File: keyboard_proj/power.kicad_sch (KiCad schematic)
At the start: 18 parts, among them IC4 USBLC6-4SC6, U1 STM32WB55CGU6, U5 918-418K2023S40026

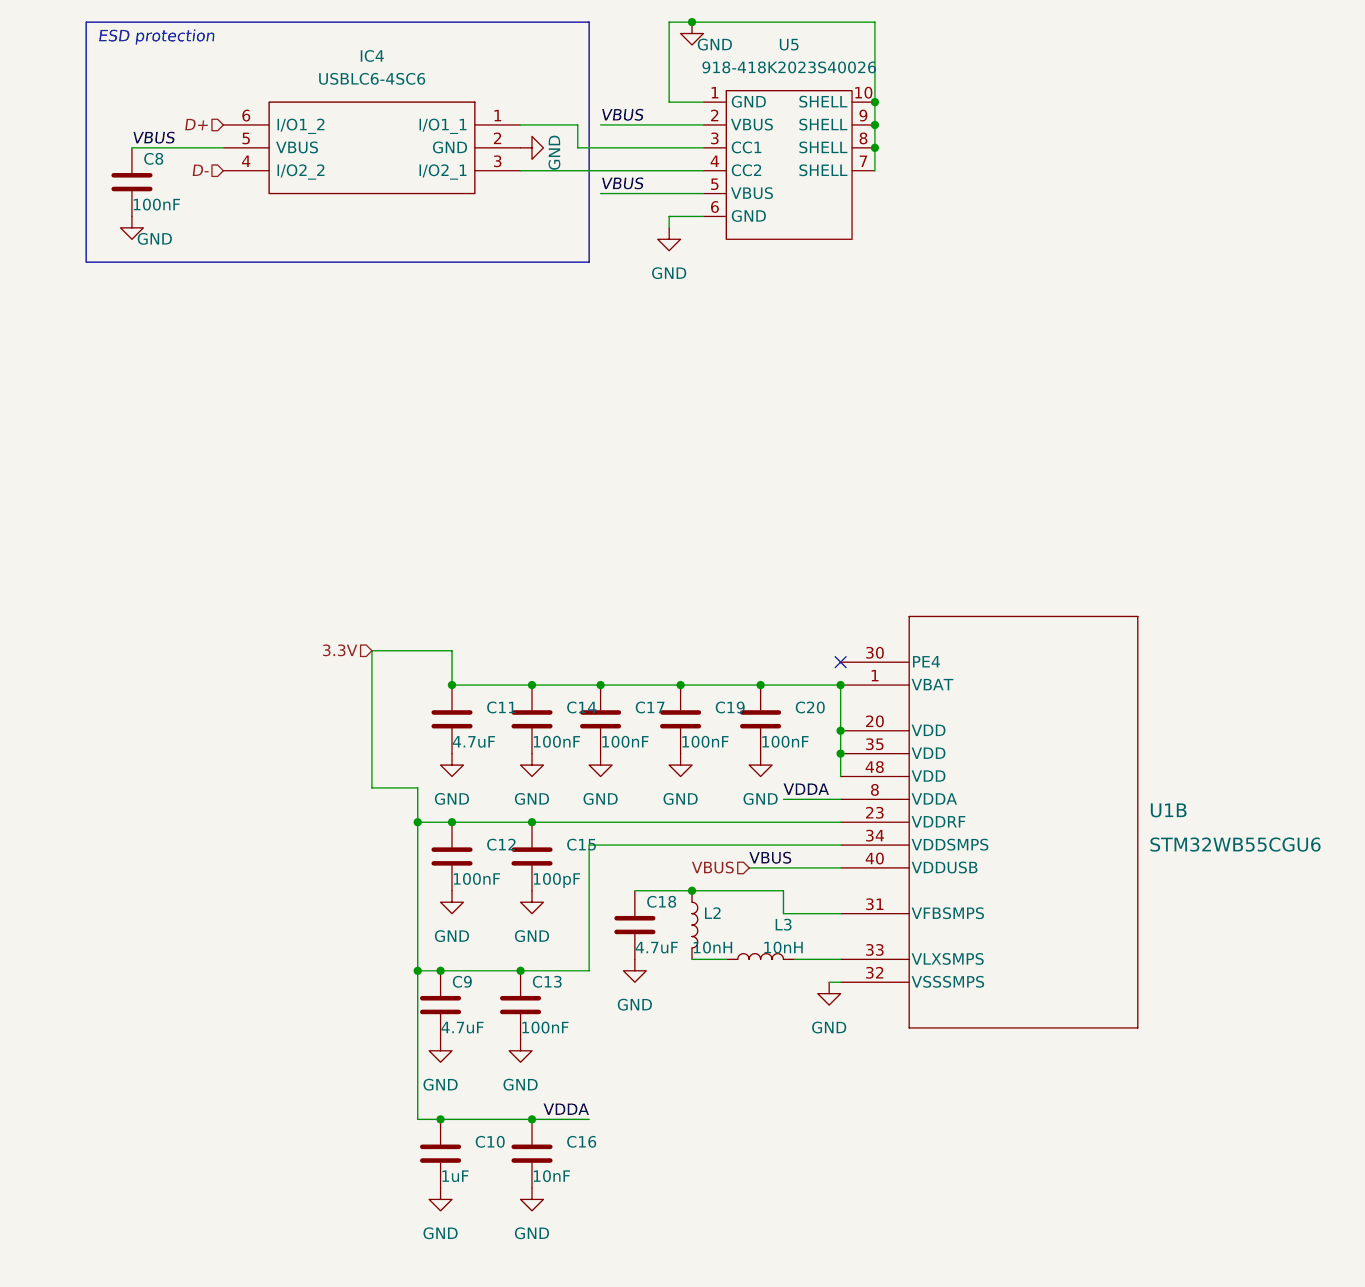
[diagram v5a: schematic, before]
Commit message: passage kicad 7, routing bien avancé
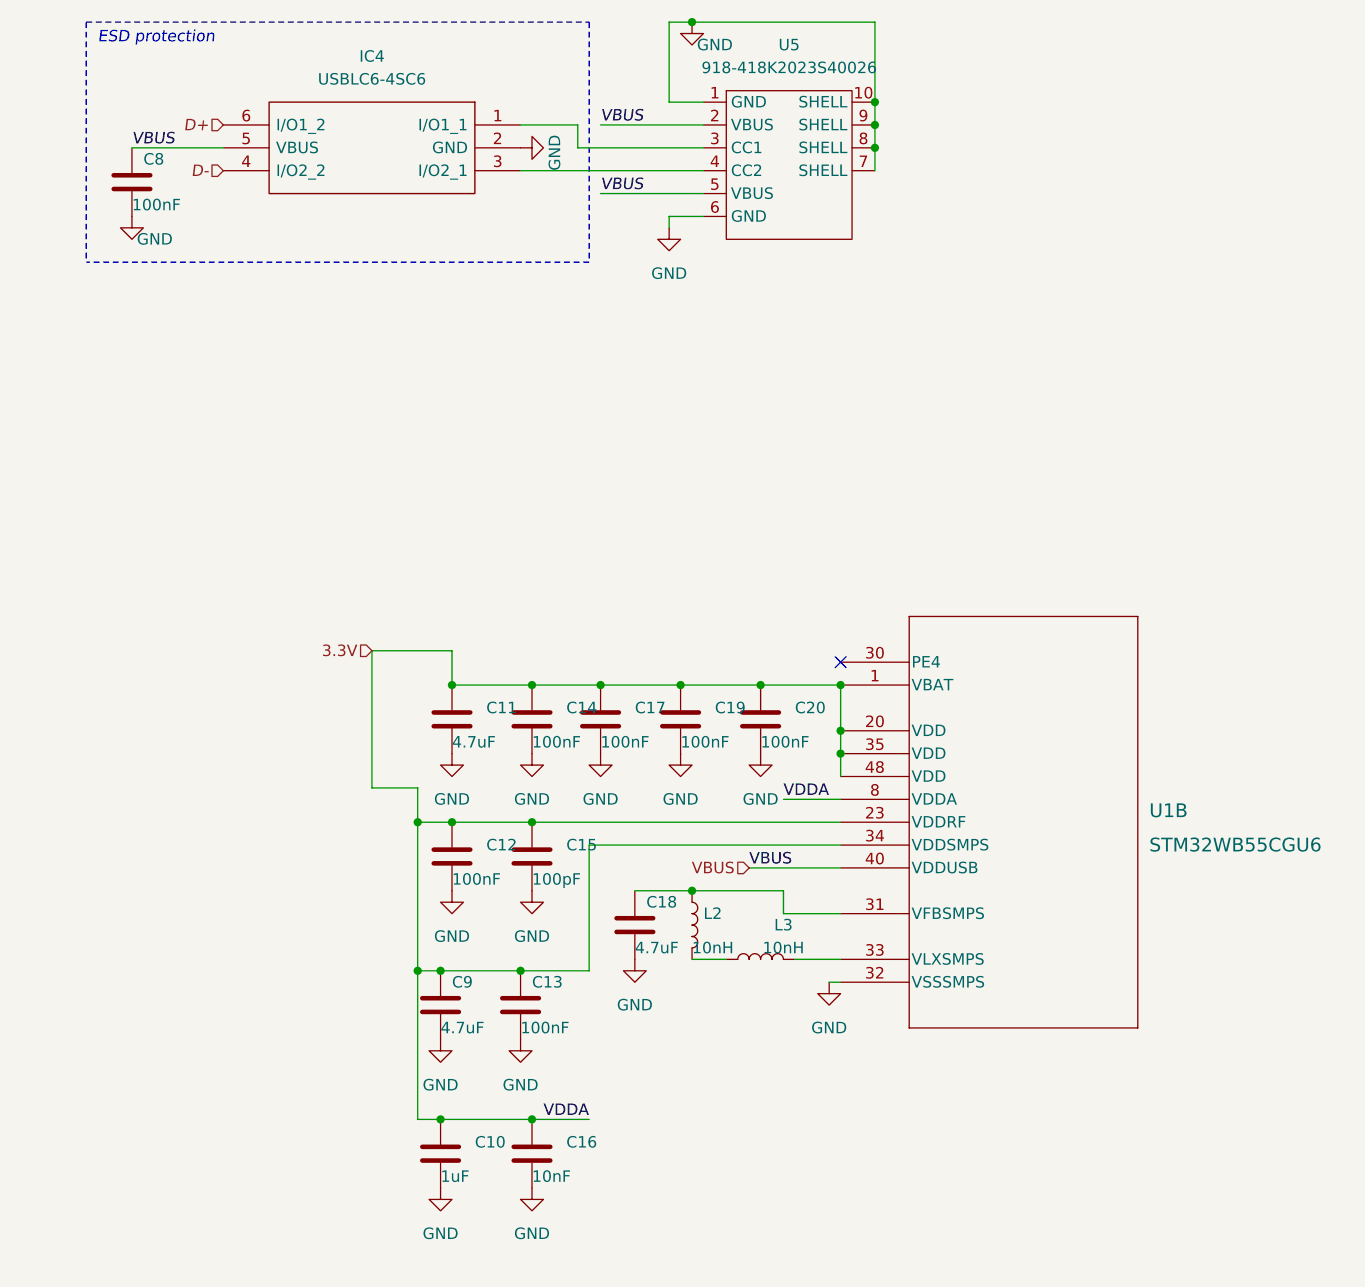
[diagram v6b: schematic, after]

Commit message: Power dlvry changée, ok mtn, routing updated
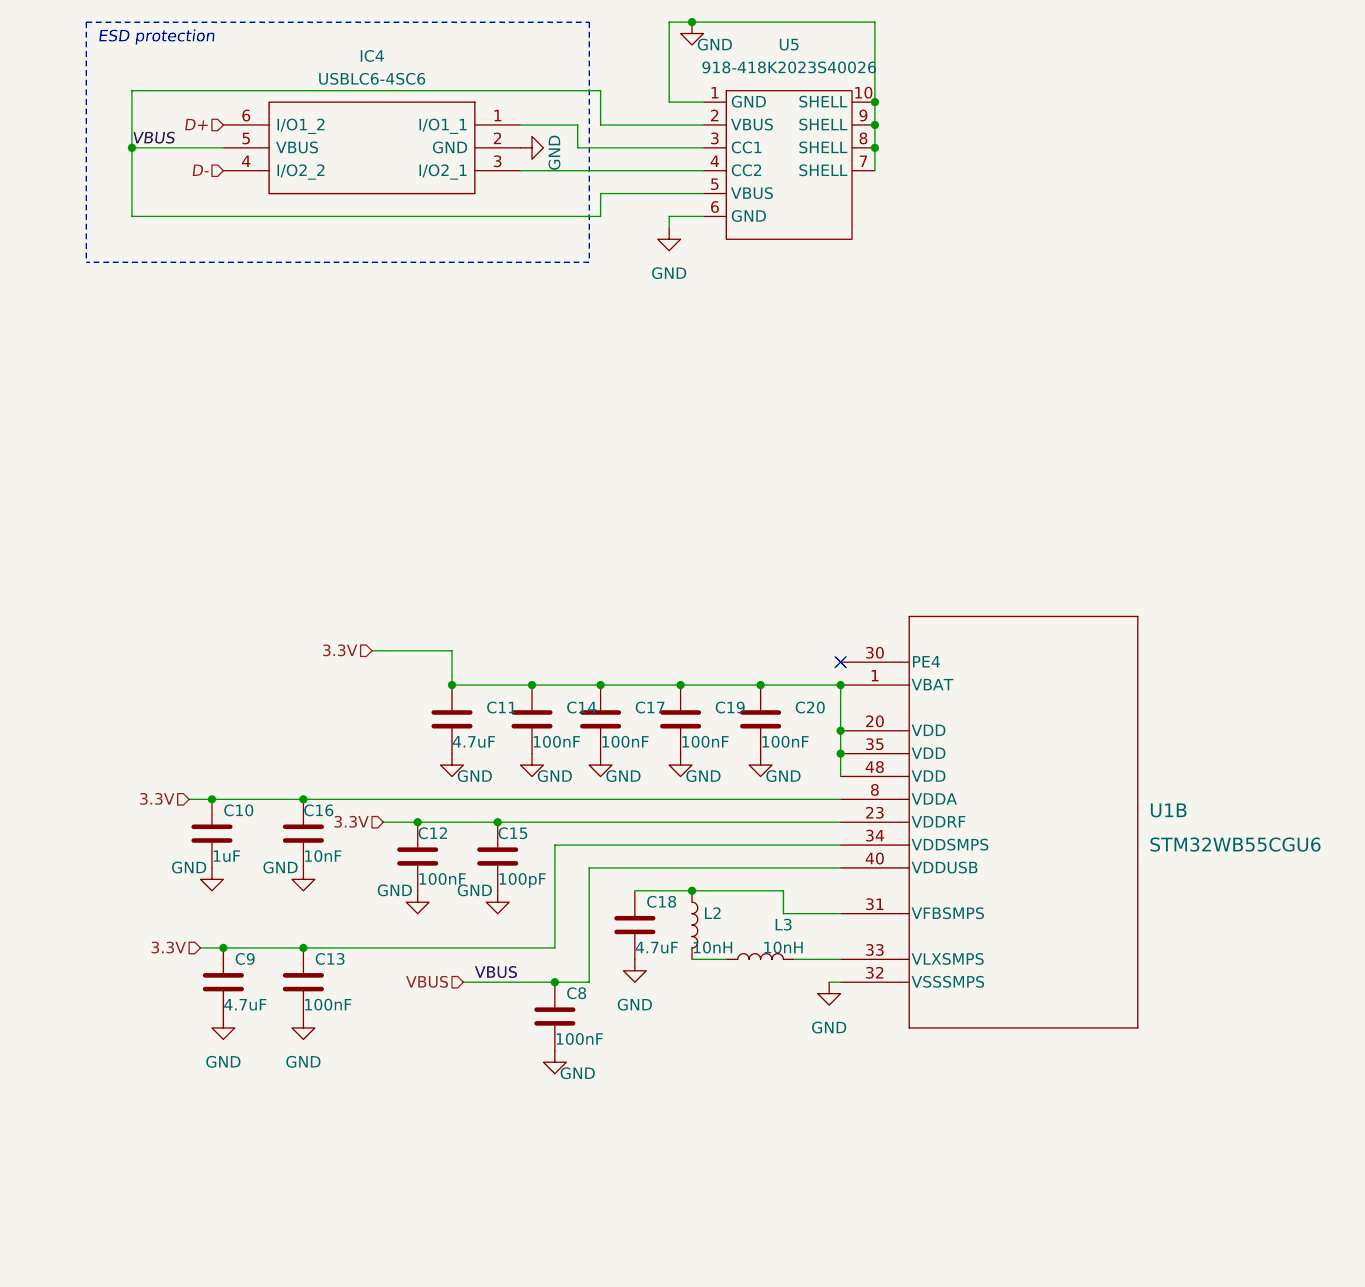
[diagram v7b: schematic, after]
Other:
- moved on the sheet: C10, C12, C15, C16

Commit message: PCB bien avancé, presque fini mais je dois selectionner des pieces de jlcpcb pour baisser les couts
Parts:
- C10: LCSC (none) -> C2887020
- C11, C18, C9: LCSC (none) -> C2874744
- C12, C13, C14, C17, C19, C20, C8: LCSC (none) -> C880603
- C15: LCSC (none) -> C5137573
- C16: LCSC (none) -> C513436
- IC4: LCSC (none) -> C5180279
- L2, L3: LCSC (none) -> C963995
- U1: LCSC (none) -> C404023
- U5: LCSC (none) -> C2763104
